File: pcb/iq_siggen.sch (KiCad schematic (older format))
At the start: 124 parts, among them J1 J3 - BANK0, J10 Barrel_Jack_MountingPin, J11 Conn_Coaxial, J12 Conn_01x01_Male, J13 Conn_01x01_Male, J14 Conn_01x01_Male, J15 Conn_01x01_Male, J16 Conn_01x01_Male, J17 Conn_01x01_Male, J2 J4 - BANK1, J3 Conn_01x10_Male, J4 Conn_01x01_Male, J5 Conn_01x10_Male, J6 Conn_Coaxial, J7 Conn_Coaxial, J8 Conn_Coaxial, J9 Conn_Coaxial, SW1 SW_Push, SW2 SW_Push, SW3 SW_Push, SW4 SW_Push, U1 AMS1117-3.3, U2 TPS72325DBVR, U3 TLV73325PDBVT

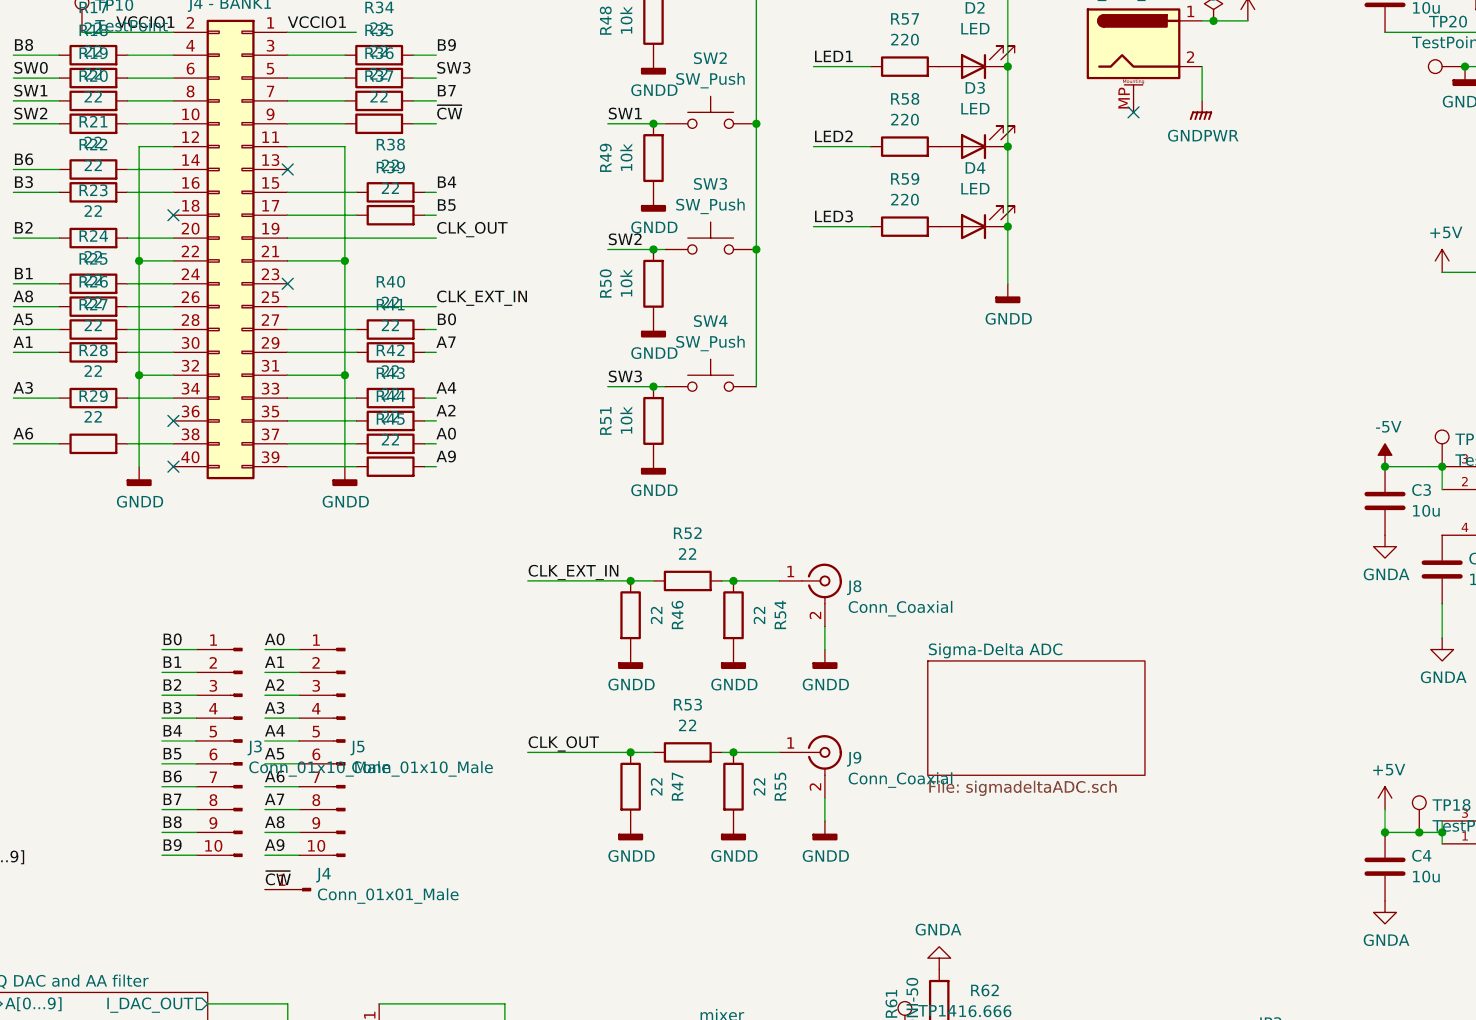
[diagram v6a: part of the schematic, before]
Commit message: route A and B channels on input connector
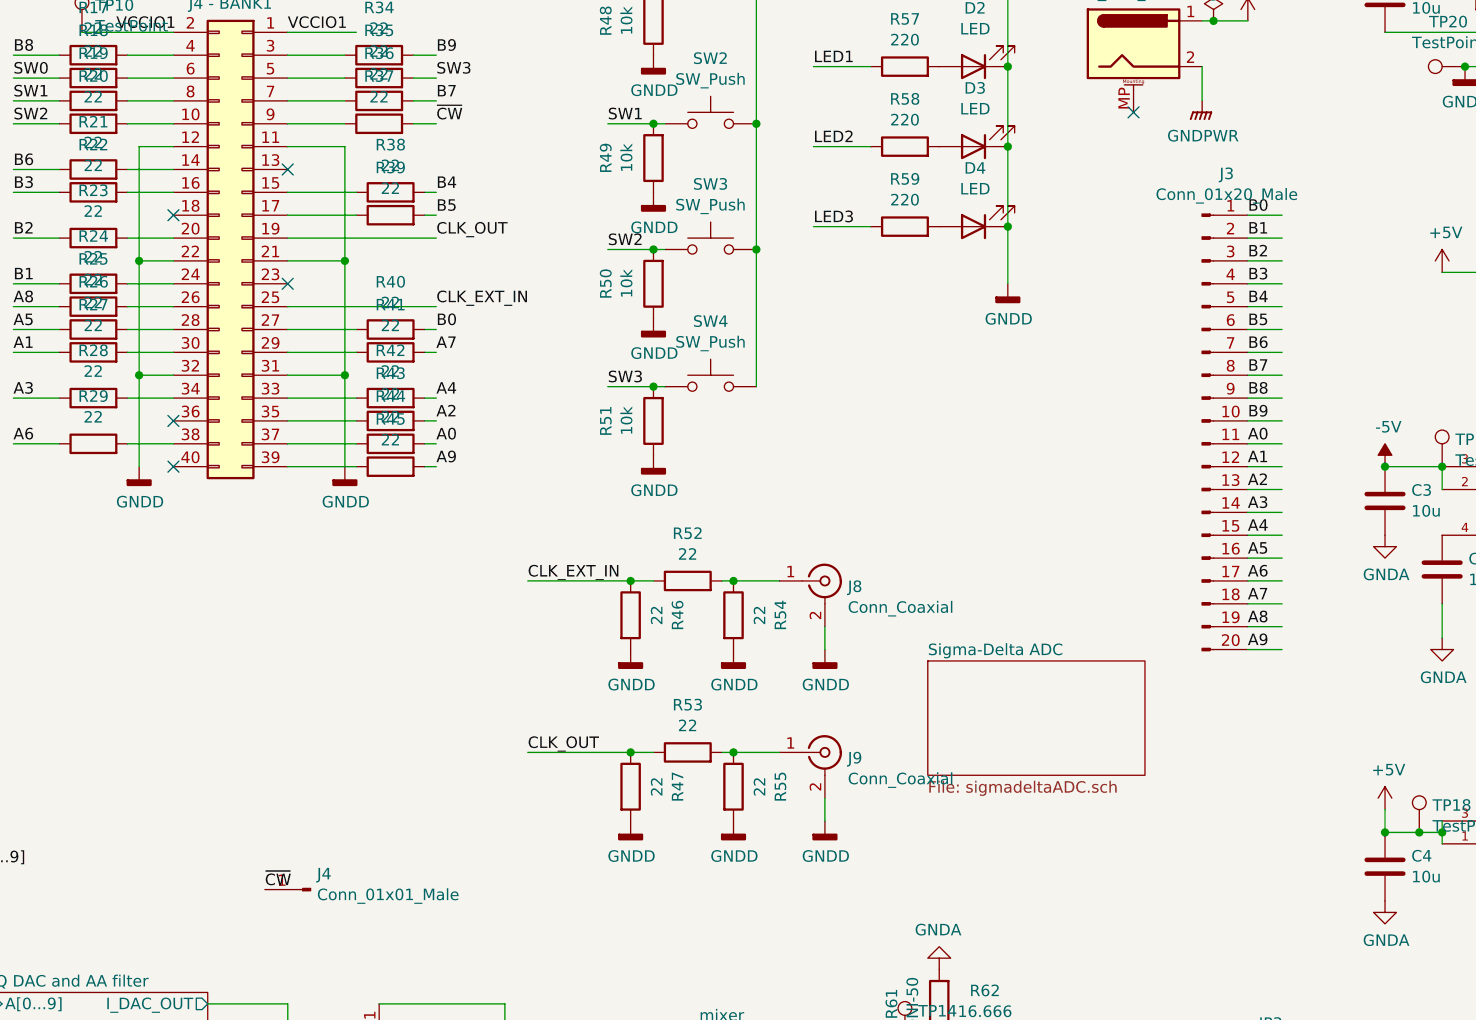
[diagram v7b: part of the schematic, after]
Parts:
- removed J3, J5: Conn_01x10_Male, Connector_PinHeader_2.54mm:PinHeader_1x10_P2.54mm_Vertical, symbol Connector:Conn_01x10_Male
- added J3: Conn_01x20_Male, Connector_PinHeader_2.54mm:PinHeader_1x20_P2.54mm_Vertical, symbol Connector:Conn_01x20_Male
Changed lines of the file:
@@
 	-1   0    0    1
-$EndComp
-Text Label 4250 3850 0    50   ~ 0
-A0
-Text Label 4250 3950 0    50   ~ 0
-A1
-Text Label 4250 4050 0    50   ~ 0
-A2
-Text Label 4250 4150 0    50   ~ 0
-A3
-Text Label 4250 4250 0    50   ~ 0
-A4
-Text Label 4250 4350 0    50   ~ 0
-A5
-Text Label 4250 4450 0    50   ~ 0
-A6
-Text Label 4250 4550 0    50   ~ 0
-A7
-Text Label 4250 4650 0    50   ~ 0
-A8
-Text Label 4250 4750 0    50   ~ 0
-A9
-Wire Wire Line
-	4250 3850 4400 3850
-Wire Wire Line
-	4250 3950 4400 3950
-Wire Wire Line
-	4250 4050 4400 4050
-Wire Wire Line
-	4250 4150 4400 4150
-Wire Wire Line
-	4250 4250 4400 4250
-Wire Wire Line
-	4250 4350 4400 4350
-Wire Wire Line
-	4250 4450 4400 4450
-Wire Wire Line
-	4250 4550 4400 4550
-Wire Wire Line
-	4250 4650 4400 4650
-Wire Wire Line
-	4250 4750 4400 4750
-Wire Wire Line
-	3800 3850 3950 3850
-Wire Wire Line
-	3800 3950 3950 3950
-Wire Wire Line
-	3800 4050 3950 4050
-Wire Wire Line
-	3800 4150 3950 4150
-Wire Wire Line
-	3800 4250 3950 4250
-Wire Wire Line
-	3800 4350 3950 4350
-Wire Wire Line
-	3800 4450 3950 4450
-Wire Wire Line
-	3800 4550 3950 4550
-Wire Wire Line
-	3800 4650 3950 4650
-Wire Wire Line
-	3800 4750 3950 4750
-Text Label 3800 3850 0    50   ~ 0
-B0
-Text Label 3800 3950 0    50   ~ 0
-B1
-Text Label 3800 4050 0    50   ~ 0
-B2
-Text Label 3800 4150 0    50   ~ 0
-B3
-Text Label 3800 4250 0    50   ~ 0
-B4
-Text Label 3800 4350 0    50   ~ 0
-B5
-Text Label 3800 4450 0    50   ~ 0
-B6
-Text Label 3800 4550 0    50   ~ 0
-B7
-Text Label 3800 4650 0    50   ~ 0
-B8
-Text Label 3800 4750 0    50   ~ 0
-B9
-$Comp
-L Connector:Conn_01x10_Male J5
-U 1 1 60A7CFCF
-P 4600 4250
-F 0 "J5" H 4572 4224 50  0000 R CNN
-F 1 "Conn_01x10_Male" H 4572 4133 50  0000 R CNN
-F 2 "Connector_PinHeader_2.54mm:PinHeader_1x10_P2.54mm_Vertical" H 4600 4250 50  0001 C CNN
-F 3 "~" H 4600 4250 50  0001 C CNN
-	1    4600 4250
-	-1   0    0    -1
-$EndComp
-$Comp
-L Connector:Conn_01x10_Male J3
-U 1 1 60A808B2
-P 4150 4250
-F 0 "J3" H 4122 4224 50  0000 R CNN
-F 1 "Conn_01x10_Male" H 4122 4133 50  0000 R CNN
-F 2 "Connector_PinHeader_2.54mm:PinHeader_1x10_P2.54mm_Vertical" H 4150 4250 50  0001 C CNN
-F 3 "~" H 4150 4250 50  0001 C CNN
-	1    4150 4250
-	-1   0    0    -1
 $EndComp
 Text Label 4250 4900 0    50   ~ 0
@@
 Wire Wire Line
 	4300 5700 4900 5700
+$Comp
+L Connector:Conn_01x20_Male J3
+U 1 1 5FC3C06B
+P 8350 2850
+F 0 "J3" H 8458 3931 50  0000 C CNN
+F 1 "Conn_01x20_Male" H 8458 3840 50  0000 C CNN
+F 2 "Connector_PinHeader_2.54mm:PinHeader_1x20_P2.54mm_Vertical" H 8350 2850 50  0001 C CNN
+F 3 "~" H 8350 2850 50  0001 C CNN
+	1    8350 2850
+	1    0    0    -1
+$EndComp
+Wire Wire Line
+	8550 1950 8700 1950
+Wire Wire Line
+	8550 2050 8700 2050
+Wire Wire Line
+	8550 2150 8700 2150
+Wire Wire Line
+	8550 2250 8700 2250
+Wire Wire Line
+	8550 2350 8700 2350
+Wire Wire Line
+	8550 2450 8700 2450
+Wire Wire Line
+	8550 2550 8700 2550
+Wire Wire Line
+	8550 2650 8700 2650
+Wire Wire Line
+	8550 2750 8700 2750
+Wire Wire Line
+	8550 2850 8700 2850
+Text Label 8550 1950 0    50   ~ 0
+B0
+Text Label 8550 2050 0    50   ~ 0
+B1
+Text Label 8550 2150 0    50   ~ 0
+B2
+Text Label 8550 2250 0    50   ~ 0
+B3
+Text Label 8550 2350 0    50   ~ 0
+B4
+Text Label 8550 2450 0    50   ~ 0
+B5
+Text Label 8550 2550 0    50   ~ 0
+B6
+Text Label 8550 2650 0    50   ~ 0
+B7
+Text Label 8550 2750 0    50   ~ 0
+B8
+Text Label 8550 2850 0    50   ~ 0
+B9
+Text Label 8550 2950 0    50   ~ 0
+A0
+Text Label 8550 3050 0    50   ~ 0
+A1
+Text Label 8550 3150 0    50   ~ 0
+A2
+Text Label 8550 3250 0    50   ~ 0
+A3
+Text Label 8550 3350 0    50   ~ 0
+A4
+Text Label 8550 3450 0    50   ~ 0
+A5
+Text Label 8550 3550 0    50   ~ 0
+A6
+Text Label 8550 3650 0    50   ~ 0
+A7
+Text Label 8550 3750 0    50   ~ 0
+A8
+Text Label 8550 3850 0    50   ~ 0
+A9
+Wire Wire Line
+	8550 2950 8700 2950
+Wire Wire Line
+	8550 3050 8700 3050
+Wire Wire Line
+	8550 3150 8700 3150
+Wire Wire Line
+	8550 3250 8700 3250
+Wire Wire Line
+	8550 3350 8700 3350
+Wire Wire Line
+	8550 3450 8700 3450
+Wire Wire Line
+	8550 3550 8700 3550
+Wire Wire Line
+	8550 3650 8700 3650
+Wire Wire Line
+	8550 3750 8700 3750
+Wire Wire Line
+	8550 3850 8700 3850
 Wire Bus Line
 	2500 3650 2500 5500

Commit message: LO amp routing
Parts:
- removed R10, R2, R3, R4: 0, Resistor_SMD:R_0603_1608Metric, symbol Device:R
- removed R11, R12, R30, R31, R5: 100, Resistor_SMD:R_0603_1608Metric, symbol Device:R
- R13, R14, R15, R16, R6, R7: value 100 -> 0
- R46, R47, R54, R55: value 22 -> DNI
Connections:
- net labels added: CLK_EXT_IN_Connector, CLK_OUT_connector
- wire segments 293 -> 275
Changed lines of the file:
@@
 Text Notes 550  5150 0    50   ~ 0
 Use LVDS-2.5V pins from bank 0 of machxo3 for all clocks
-Wire Wire Line
-	2500 2400 2350 2400
 $Comp
 L Device:R R6
@@
 P 1500 5500
 F 0 "R6" V 1707 5500 50  0000 C CNN
-F 1 "100" V 1616 5500 50  0000 C CNN
+F 1 "0" V 1616 5500 50  0000 C CNN
 F 2 "Resistor_SMD:R_0603_1608Metric" V 1430 5500 50  0001 C CNN
 F 3 "~" H 1500 5500 50  0001 C CNN
@@
 P 1500 5900
 F 0 "R7" V 1293 5900 50  0000 C CNN
-F 1 "100" V 1384 5900 50  0000 C CNN
+F 1 "0" V 1384 5900 50  0000 C CNN
 F 2 "Resistor_SMD:R_0603_1608Metric" V 1430 5900 50  0001 C CNN
 F 3 "~" H 1500 5900 50  0001 C CNN
@@
 	0    1    1    0
 $EndComp
-$Comp
-L Device:R R8
-U 1 1 5FE74C1A
-P 1750 5700
-F 0 "R8" H 1680 5654 50  0000 R CNN
-F 1 "100" H 1680 5745 50  0000 R CNN
-F 2 "Resistor_SMD:R_0603_1608Metric" V 1680 5700 50  0001 C CNN
-F 3 "~" H 1750 5700 50  0001 C CNN
-	1    1750 5700
-	-1   0    0    1
-$EndComp
-$Comp
-L Device:R R5
-U 1 1 5FE76ECD
-P 1250 5700
-F 0 "R5" H 1320 5746 50  0000 L CNN
-F 1 "100" H 1320 5655 50  0000 L CNN
-F 2 "Resistor_SMD:R_0603_1608Metric" V 1180 5700 50  0001 C CNN
-F 3 "~" H 1250 5700 50  0001 C CNN
-	1    1250 5700
-	1    0    0    -1
-$EndComp
 Wire Wire Line
 	700  5500 1250 5500
@@
 Wire Wire Line
 	1750 5500 1750 5550
-Wire Wire Line
-	1250 5550 1250 5500
 Connection ~ 1250 5500
 Wire Wire Line
 	1250 5500 1350 5500
-Wire Wire Line
-	1250 5850 1250 5900
 Connection ~ 1250 5900
 Wire Wire Line
@@
 P 3350 6450
 F 0 "R13" V 3557 6450 50  0000 C CNN
-F 1 "100" V 3466 6450 50  0000 C CNN
+F 1 "0" V 3466 6450 50  0000 C CNN
 F 2 "Resistor_SMD:R_0603_1608Metric" V 3280 6450 50  0001 C CNN
 F 3 "~" H 3350 6450 50  0001 C CNN
@@
 P 3350 6850
 F 0 "R14" V 3143 6850 50  0000 C CNN
-F 1 "100" V 3234 6850 50  0000 C CNN
+F 1 "0" V 3234 6850 50  0000 C CNN
 F 2 "Resistor_SMD:R_0603_1608Metric" V 3280 6850 50  0001 C CNN
 F 3 "~" H 3350 6850 50  0001 C CNN
@@
 	0    1    1    0
 $EndComp
-$Comp
-L Device:R R30
-U 1 1 5FEA51D1
-P 3600 6650
-F 0 "R30" H 3530 6604 50  0000 R CNN
-F 1 "100" H 3530 6695 50  0000 R CNN
-F 2 "Resistor_SMD:R_0603_1608Metric" V 3530 6650 50  0001 C CNN
-F 3 "~" H 3600 6650 50  0001 C CNN
-	1    3600 6650
-	-1   0    0    1
-$EndComp
-$Comp
-L Device:R R11
-U 1 1 5FEA51D7
-P 3100 6650
-F 0 "R11" H 3170 6696 50  0000 L CNN
-F 1 "100" H 3170 6605 50  0000 L CNN
-F 2 "Resistor_SMD:R_0603_1608Metric" V 3030 6650 50  0001 C CNN
-F 3 "~" H 3100 6650 50  0001 C CNN
-	1    3100 6650
-	1    0    0    -1
-$EndComp
 Wire Wire Line
 	2800 6450 3100 6450
 Wire Wire Line
 	2800 6850 3100 6850
-Wire Wire Line
-	3500 6850 3600 6850
-Wire Wire Line
-	3600 6850 3600 6800
-Wire Wire Line
-	3500 6450 3600 6450
-Wire Wire Line
-	3600 6450 3600 6500
-Wire Wire Line
-	3100 6500 3100 6450
 Connection ~ 3100 6450
 Wire Wire Line
 	3100 6450 3200 6450
-Wire Wire Line
-	3100 6800 3100 6850
 Connection ~ 3100 6850
 Wire Wire Line
@@
 	3800 6600 3800 6450
 Wire Wire Line
-	3800 6450 3600 6450
-Connection ~ 3600 6450
-Wire Wire Line
 	3800 6700 4900 6700
-Connection ~ 3600 6850
-Wire Wire Line
-	3800 6850 3600 6850
 Wire Wire Line
 	3800 6700 3800 6850
@@
 P 3350 7200
 F 0 "R15" V 3557 7200 50  0000 C CNN
-F 1 "100" V 3466 7200 50  0000 C CNN
+F 1 "0" V 3466 7200 50  0000 C CNN
 F 2 "Resistor_SMD:R_0603_1608Metric" V 3280 7200 50  0001 C CNN
 F 3 "~" H 3350 7200 50  0001 C CNN
@@
 P 3350 7600
 F 0 "R16" V 3143 7600 50  0000 C CNN
-F 1 "100" V 3234 7600 50  0000 C CNN
+F 1 "0" V 3234 7600 50  0000 C CNN
 F 2 "Resistor_SMD:R_0603_1608Metric" V 3280 7600 50  0001 C CNN
 F 3 "~" H 3350 7600 50  0001 C CNN
@@
 	0    1    1    0
 $EndComp
-$Comp
-L Device:R R31
-U 1 1 5FEE5DDD
-P 3600 7400
-F 0 "R31" H 3530 7354 50  0000 R CNN
-F 1 "100" H 3530 7445 50  0000 R CNN
-F 2 "Resistor_SMD:R_0603_1608Metric" V 3530 7400 50  0001 C CNN
-F 3 "~" H 3600 7400 50  0001 C CNN
-	1    3600 7400
-	-1   0    0    1
-$EndComp
-$Comp
-L Device:R R12
-U 1 1 5FEE5DE3
-P 3100 7400
-F 0 "R12" H 3170 7446 50  0000 L CNN
-F 1 "100" H 3170 7355 50  0000 L CNN
-F 2 "Resistor_SMD:R_0603_1608Metric" V 3030 7400 50  0001 C CNN
-F 3 "~" H 3100 7400 50  0001 C CNN
-	1    3100 7400
-	1    0    0    -1
-$EndComp
 Wire Wire Line
 	2800 7200 3100 7200
 Wire Wire Line
 	2800 7600 3100 7600
-Wire Wire Line
-	3500 7600 3600 7600
-Wire Wire Line
-	3600 7600 3600 7550
-Wire Wire Line
-	3500 7200 3600 7200
-Wire Wire Line
-	3600 7200 3600 7250
-Wire Wire Line
-	3100 7250 3100 7200
 Connection ~ 3100 7200
 Wire Wire Line
 	3100 7200 3200 7200
-Wire Wire Line
-	3100 7550 3100 7600
 Connection ~ 3100 7600
 Wire Wire Line
@@
 Wire Wire Line
 	3800 7350 3800 7200
-Wire Wire Line
-	3800 7200 3600 7200
-Connection ~ 3600 7200
-Connection ~ 3600 7600
-Wire Wire Line
-	3800 7600 3600 7600
 Wire Wire Line
 	3800 7450 3800 7600
@@
 Text Label 500  2500 0    50   ~ 0
 I_CLK_P
-Wire Wire Line
-	500  2500 900  2500
 Text Label 2500 2400 0    50   ~ 0
 I_CLK_N
 Text Label 500  1900 0    50   ~ 0
 Q_CLK_P
-Wire Wire Line
-	500  1900 900  1900
 Text Label 500  1800 0    50   ~ 0
 Q_CLK_N
-Wire Wire Line
-	500  1800 900  1800
 Text Notes 1000 700  0    50   ~ 0
 See FPGA-board pinmap.xlsx for pin mapping
@@
 	2050 1500 1950 1500
 $Comp
-L Device:R R10
-U 1 1 6063E7B3
-P 2200 2400
-F 0 "R10" V 2407 2400 50  0000 C CNN
-F 1 "0" V 2316 2400 50  0000 C CNN
-F 2 "Resistor_SMD:R_0603_1608Metric" V 2130 2400 50  0001 C CNN
-F 3 "~" H 2200 2400 50  0001 C CNN
-	1    2200 2400
-	0    -1   -1   0
-$EndComp
-Wire Wire Line
-	2050 2400 1950 2400
-$Comp
-L Device:R R4
-U 1 1 6065CD56
-P 1050 2500
-F 0 "R4" V 1257 2500 50  0000 C CNN
-F 1 "0" V 1166 2500 50  0000 C CNN
-F 2 "Resistor_SMD:R_0603_1608Metric" V 980 2500 50  0001 C CNN
-F 3 "~" H 1050 2500 50  0001 C CNN
-	1    1050 2500
-	0    -1   -1   0
-$EndComp
-Wire Wire Line
-	1200 2500 1450 2500
-$Comp
-L Device:R R3
-U 1 1 6065D190
-P 1050 1900
-F 0 "R3" V 1257 1900 50  0000 C CNN
-F 1 "0" V 1166 1900 50  0000 C CNN
-F 2 "Resistor_SMD:R_0603_1608Metric" V 980 1900 50  0001 C CNN
-F 3 "~" H 1050 1900 50  0001 C CNN
-	1    1050 1900
-	0    -1   -1   0
-$EndComp
-Wire Wire Line
-	1200 1900 1450 1900
-$Comp
-L Device:R R2
-U 1 1 6065D5B1
-P 1050 1800
-F 0 "R2" V 1257 1800 50  0000 C CNN
-F 1 "0" V 1166 1800 50  0000 C CNN
-F 2 "Resistor_SMD:R_0603_1608Metric" V 980 1800 50  0001 C CNN
-F 3 "~" H 1050 1800 50  0001 C CNN
-	1    1050 1800
-	0    -1   -1   0
-$EndComp
-Wire Wire Line
-	1200 1800 1450 1800
-$Comp
 L Device:R R1
 U 1 1 6065D95A
@@
 	1    0    0    -1
 $EndComp
-$Comp
-L Device:R R52
-U 1 1 6083678B
-P 6100 3550
-F 0 "R52" V 6307 3550 50  0000 C CNN
-F 1 "22" V 6216 3550 50  0000 C CNN
-F 2 "Resistor_SMD:R_0603_1608Metric" V 6030 3550 50  0001 C CNN
-F 3 "~" H 6100 3550 50  0001 C CNN
-	1    6100 3550
-	0    -1   -1   0
-$EndComp
 Wire Wire Line
 	6500 3550 6300 3550
@@
 P 6300 3700
 F 0 "R54" V 6507 3700 50  0000 C CNN
-F 1 "22" V 6416 3700 50  0000 C CNN
+F 1 "DNI" V 6416 3700 50  0000 C CNN
 F 2 "Resistor_SMD:R_0603_1608Metric" V 6230 3700 50  0001 C CNN
 F 3 "~" H 6300 3700 50  0001 C CNN
@@
 P 5850 3700
 F 0 "R46" V 6057 3700 50  0000 C CNN
-F 1 "22" V 5966 3700 50  0000 C CNN
+F 1 "DNI" V 5966 3700 50  0000 C CNN
 F 2 "Resistor_SMD:R_0603_1608Metric" V 5780 3700 50  0001 C CNN
 F 3 "~" H 5850 3700 50  0001 C CNN
@@
 P 6300 4450
 F 0 "R55" V 6507 4450 50  0000 C CNN
-F 1 "22" V 6416 4450 50  0000 C CNN
+F 1 "DNI" V 6416 4450 50  0000 C CNN
 F 2 "Resistor_SMD:R_0603_1608Metric" V 6230 4450 50  0001 C CNN
 F 3 "~" H 6300 4450 50  0001 C CNN
@@
 P 5850 4450
 F 0 "R47" V 6057 4450 50  0000 C CNN
-F 1 "22" V 5966 4450 50  0000 C CNN
+F 1 "DNI" V 5966 4450 50  0000 C CNN
 F 2 "Resistor_SMD:R_0603_1608Metric" V 5780 4450 50  0001 C CNN
 F 3 "~" H 5850 4450 50  0001 C CNN
@@
 Wire Wire Line
 	8550 3850 8700 3850
+Text Label 6400 3550 0    50   ~ 0
+CLK_EXT_IN_Connector
+Text Label 6400 4300 0    50   ~ 0
+CLK_OUT_connector
+Wire Wire Line
+	3500 7200 3800 7200
+Wire Wire Line
+	3500 7600 3800 7600
+Wire Wire Line
+	3500 6850 3800 6850
+Wire Wire Line
+	3500 6450 3800 6450
+Wire Wire Line
+	1950 2400 2500 2400
+Wire Wire Line
+	500  2500 1450 2500
+Wire Wire Line
+	500  1800 1450 1800
+Wire Wire Line
+	500  1900 1450 1900
+$Comp
+L Device:R R52
+U 1 1 6083678B
+P 6100 3550
+F 0 "R52" V 6307 3550 50  0000 C CNN
+F 1 "22" V 6216 3550 50  0000 C CNN
+F 2 "Resistor_SMD:R_0603_1608Metric" V 6030 3550 50  0001 C CNN
+F 3 "~" H 6100 3550 50  0001 C CNN
+	1    6100 3550
+	0    -1   -1   0
+$EndComp
 Wire Bus Line
 	2500 3650 2500 5500
 Wire Bus Line
 	2950 3650 2950 5400
+$Comp
+L Device:R R8
+U 1 1 5FE74C1A
+P 1750 5700
+F 0 "R8" H 1680 5654 50  0000 R CNN
+F 1 "100" H 1680 5745 50  0000 R CNN
+F 2 "Resistor_SMD:R_0603_1608Metric" V 1680 5700 50  0001 C CNN
+F 3 "~" H 1750 5700 50  0001 C CNN
+	1    1750 5700
+	-1   0    0    1
+$EndComp
 $EndSCHEMATC
